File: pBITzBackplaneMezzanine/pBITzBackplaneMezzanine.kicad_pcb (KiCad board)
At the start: 4 copper layers, 99.9 x 80.4 mm, 43 parts, among them J1 USB3_A_Stacked, J2 Conn_01x04, J3 Conn_01x04, J4 10067847-001RLF, J5 Conn_02x10_Odd_Even, U1 FE1.1S-BSOP28BCN, U2 MAX3421EETJ_T, U3 CD74HC4050M96, U4 CD74HC4050M96, Y1 ABL-12.000MHZ-B2, Y2 ABL-12.000MHZ-B2

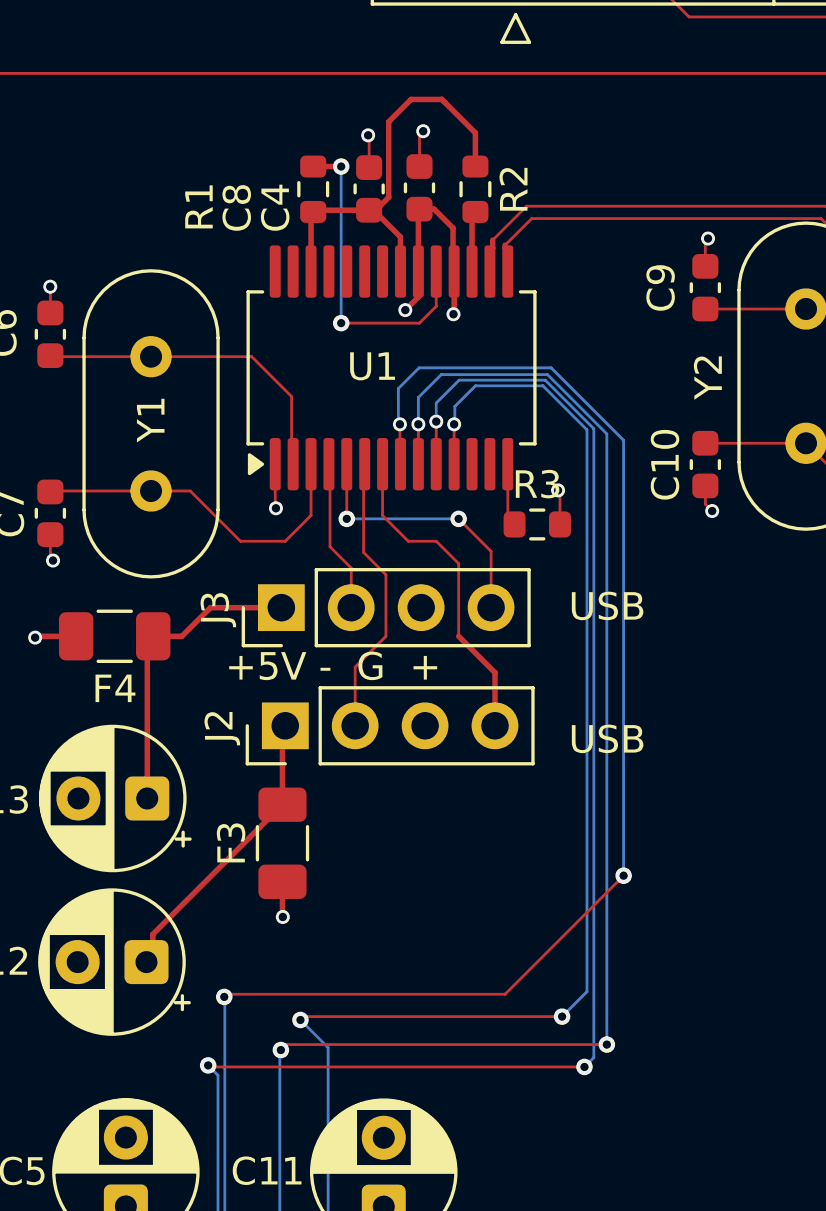
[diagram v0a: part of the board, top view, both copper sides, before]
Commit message: Fixed the footprint for the FE1.1
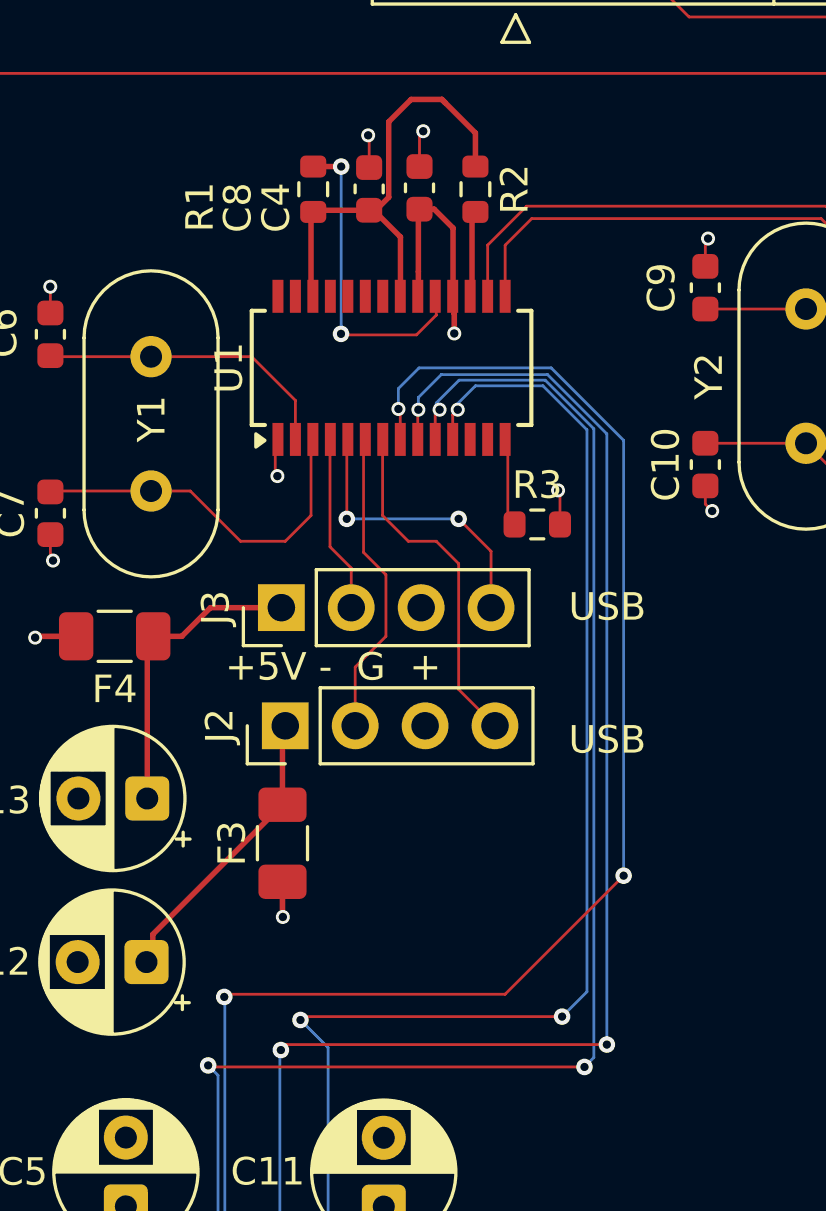
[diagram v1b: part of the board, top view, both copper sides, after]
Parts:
- U1: footprint Package_SO:SSOP-28_5.3x10.2mm_P0.65mm -> Package_SO:SSOP-28_3.9x9.9mm_P0.635mm
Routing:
- net +3V3_INTERNAL: track 15.5 -> 17.3 mm
- net /USBPorts/D+: track 23.9 -> 25.6 mm
- net /USBPorts/D-: track 25.0 -> 26.6 mm
- net /USBPorts/DM3: track 10.3 -> 11.2 mm
- net /USBPorts/DM4: track 5.49 -> 6.44 mm
- net Net-(U1-REXT): track 1.94 -> 2.88 mm
- net Net-(U1-XIN): track 12.4 -> 13.4 mm
- net Net-(U1-XRSTJ): track 2.04 -> 2.97 mm
- net /USBPorts/DP4: track 9.76 -> 10.7 mm
- net /USBPorts/DP3: track 11.8 -> 12.7 mm
- net /USBPorts/DP2: track 58.9 -> 58.0 mm
- net /USBPorts/DM2: track 60.7 -> 59.8 mm
- net /USBPorts/DP1: track 58.8 -> 58.0 mm
- net /USBPorts/DM1: track 63.6 -> 62.8 mm
- net +5V: track 14.2 -> 13.6 mm, vias 6 -> 5
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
